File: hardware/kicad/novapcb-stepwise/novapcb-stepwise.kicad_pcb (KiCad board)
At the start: 6 copper layers, 105 x 85 mm, 129 parts, among them J1 USB-C_2.0, J10 CRSF_solder_pad, J11 ESC_solder_pad, J12 ESC_solder_pad, J13 ESC_solder_pad, J14 ESC_solder_pad, J15 ESC_solder_pad, J16 ESC_solder_pad, J17 ESC_solder_pad, J18 ESC_solder_pad, J19 MAUCH2_6P, J2 microSD_DM3AT, J20 CAN_4P, J3 TELEM_6P, J4 MAUCH_6P, J5 GPS_MAG_10P, J9 SWD_10P, Q2 AO3401A, Q3 AO4262E, Q4 AO4262E, Q5 AO3400A, U1 STM32H743VITx, U11 LM74700-Q1, U12 LM74700-Q1, U13 LP5907MFX-3.3, U14 TJA1051TK/3, U15 PESD2CAN, U2 AP2112K-3.3, U3 ICM-42688-P_LGA-14_2.5x3mm_P0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, U4 DPS310, U5 USBLC6-2P6, U6 TPS25940A, U7 LPS22HB, U8 BMI088, U9 LSM6DSV16X, Y1 8MHz

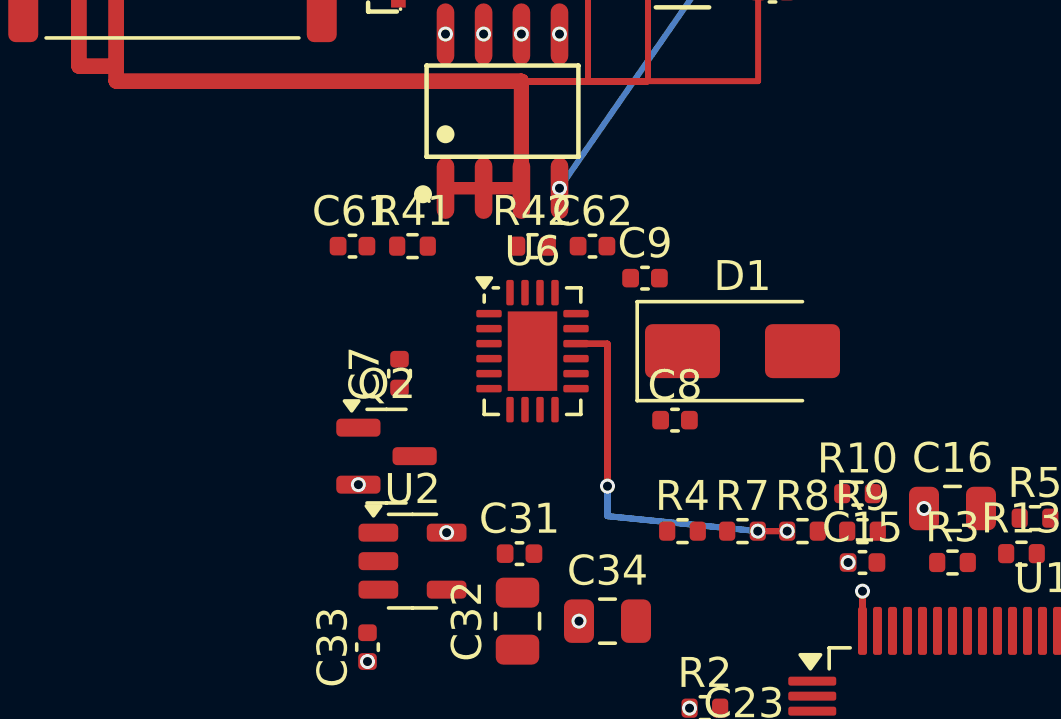
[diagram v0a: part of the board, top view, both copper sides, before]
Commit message: hw: R42/C62 west-relocate per master Option (selective B re-place)
Per master 2026-05-23 selective relocation approval after routing-
aware-density paper analysis.

## Move
  R42: (28.00, 14.50) → (20.00, 14.50) — 8mm west
  C62: (30.00, 14.50) → (18.00, 14.50) — 12mm west

Both moves CLEAR X=27..30 strip at Y=14.5 (U6's north-pin exit
column).

## Routing-aware-density verification (paper, executed pre-move)
All 4 EFUSE routes verified geometrically possible with new positions
in the basic-clearance sense. R42 no longer blocks DVDT/ILIM/FLT exits.

## Post-execute DRC: 11 violations (down from blocked)

Sense-row blockers RESOLVED. But other geometric conflicts surfaced
that the basic-clearance verification missed:
  - OVP F.Cu trace at X=31.5 too close to D1 pad west edge 31.75
    (gap 0.15mm vs 0.20mm rule). Needs via X<31.45.
  - ILIM B.Cu diagonal (28.75, 14.5)→(32.49, 24) passes within
    0.37mm of OVP via center at (31.5, 22.5) — 0.02mm edge-to-edge
    fail.
  - DVDT via at (28.25, 13) too close to Q3.3 pad (27.63, 12.57)
    — 0.75mm vs 1.05mm clearance need (via 0.25 + pad 0.6 + clr 0.2).
  - ILIM via at (28.75, 14.5) too close to DVDT F.Cu at X=28.25
    Y=14.5 (gap 0.15mm via-to-track edge).
  - EN B.Cu vs ILIM B.Cu cross in R-corridor.

These are SECOND-ORDER conflicts (placement of R42/C62 was the
first-order; now the routing-routing collisions and Q3/D1 adjacency
need addressing).

ESCALATING — multiple targeted routing iterations needed OR more
placement nudges (R4 east, OVP via re-position, etc).

## Sequence ask
Master direction needed on iteration approach: keep iterating routing
under no-new-fab-exceptions rule, or pause and assess whether one
more bounded placement change resolves all 4 cleanly.

Co-Authored-By: Claude Opus 4.7 <noreply@anthropic.com>
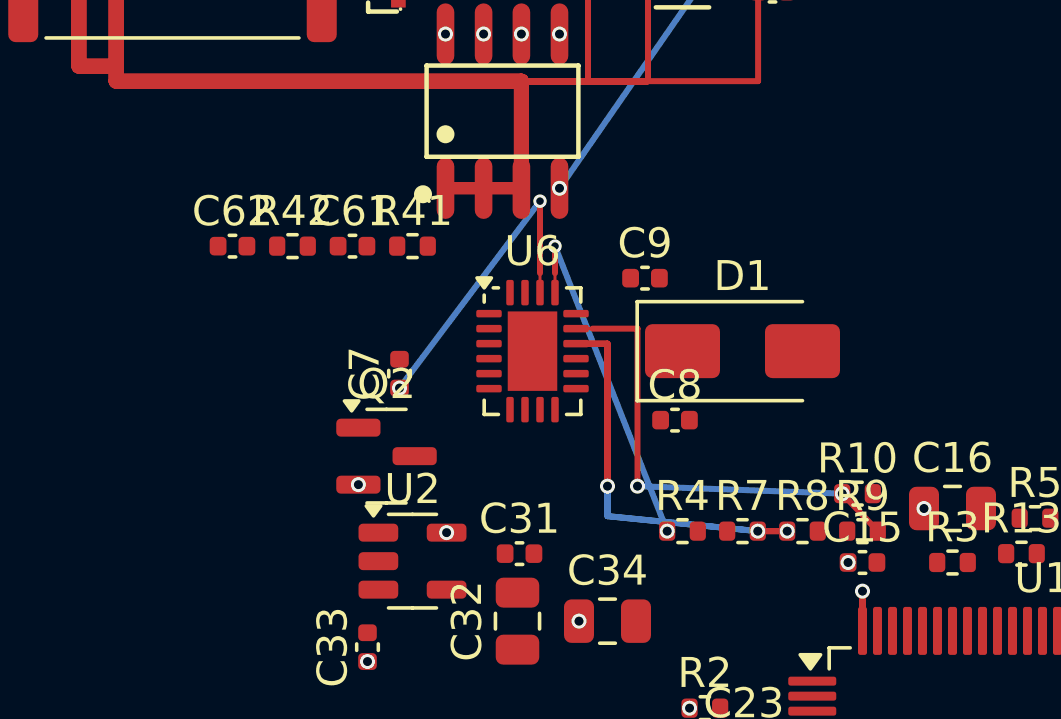
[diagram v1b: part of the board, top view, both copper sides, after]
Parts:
- moved C62 12.0 mm to (18.0, 14.5)
- moved R42 8.00 mm to (20.0, 14.5)
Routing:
- net EFUSE_OVP: track 0.00 -> 15.9 mm, vias 0 -> 2
- net EFUSE_ILIM: track 0.00 -> 11.8 mm, vias 0 -> 2
- net EFUSE_DVDT: track 0.00 -> 10.8 mm, vias 0 -> 2
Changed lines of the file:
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@@
 	(footprint "Capacitor_SMD:C_0402_1005Metric"
 		(layer "F.Cu")
-		(at 30 14.5)
+		(at 18 14.5)
 		(descr "Capacitor SMD 0402 (1005 Metric), square (rectangular) end terminal, IPC-7351 nominal, (Body size source: IPC-SM-782 page 76, https://www.pcb-3d.com/wordpress/wp-content/uploads/ipc-sm-782a_amendment_1_and_2.pdf), generated with kicad-footprint-generator")
 		(tags "capacitor")
@@
 	(footprint "Resistor_SMD:R_0402_1005Metric"
 		(layer "F.Cu")
-		(at 28 14.5)
+		(at 20 14.5)
 		(descr "Resistor SMD 0402 (1005 Metric), square (rectangular) end terminal, IPC-7351 nominal, (Body size source: IPC-SM-782 page 72, https://www.pcb-3d.com/wordpress/wp-content/uploads/ipc-sm-782a_amendment_1_and_2.pdf), generated with kicad-footprint-generator")
 		(tags "resistor")
@@
 	)
 	(segment
+		(start 28.25 16.05)
+		(end 28.25 15.4)
+		(width 0.1)
+		(layer "F.Cu")
+		(net 23)
+	)
+	(segment
+		(start 28.25 15.4)
+		(end 28.25 13)
+		(width 0.2)
+		(layer "F.Cu")
+		(net 23)
+	)
+	(via
+		(at 23.566987 19.23)
+		(size 0.5)
+		(drill 0.3)
+		(layers "F.Cu" "B.Cu")
+		(net 23)
+	)
+	(via
+		(at 28.25 13)
+		(size 0.45)
+		(drill 0.25)
+		(layers "F.Cu" "B.Cu")
+		(net 23)
+	)
+	(segment
+		(start 28.25 13)
+		(end 23.566987 19.23)
+		(width 0.2)
+		(layer "B.Cu")
+		(net 23)
+	)
+	(segment
 		(start 29.45 17.75)
 		(end 30.5 17.75)
@@
 	)
 	(segment
+		(start 28.75 16.05)
+		(end 28.75 15.4)
+		(width 0.1)
+		(layer "F.Cu")
+		(net 26)
+	)
+	(segment
+		(start 28.75 15.4)
+		(end 28.75 14.5)
+		(width 0.2)
+		(layer "F.Cu")
+		(net 26)
+	)
+	(via
+		(at 28.75 14.5)
+		(size 0.45)
+		(drill 0.25)
+		(layers "F.Cu" "B.Cu")
+		(net 26)
+	)
+	(via
+		(at 32.49 24)
+		(size 0.5)
+		(drill 0.3)
+		(layers "F.Cu" "B.Cu")
+		(net 26)
+	)
+	(segment
+		(start 28.75 14.5)
+		(end 32.49 24)
+		(width 0.2)
+		(layer "B.Cu")
+		(net 26)
+	)
+	(segment
+		(start 30 17.25)
+		(end 31.5 17.25)
+		(width 0.2)
+		(layer "F.Cu")
+		(net 27)
+	)
+	(segment
+		(start 31.5 17.25)
+		(end 31.5 22.5)
+		(width 0.2)
+		(layer "F.Cu")
+		(net 27)
+	)
+	(segment
+		(start 38.324936 22.75)
+		(end 39.51 24)
+		(width 0.2)
+		(layer "F.Cu")
+		(net 27)
+	)
+	(segment
+		(start 29.45 17.25)
+		(end 30 17.25)
+		(width 0.1)
+		(layer "F.Cu")
+		(net 27)
+	)
+	(via
+		(at 31.5 22.5)
+		(size 0.5)
+		(drill 0.3)
+		(layers "F.Cu" "B.Cu")
+		(net 27)
+	)
+	(via
+		(at 38.324936 22.75)
+		(size 0.5)
+		(drill 0.3)
+		(layers "F.Cu" "B.Cu")
+		(net 27)
+	)
+	(segment
+		(start 31.5 22.5)
+		(end 38.324936 22.75)
+		(width 0.2)
+		(layer "B.Cu")
+		(net 27)
+	)
+	(segment

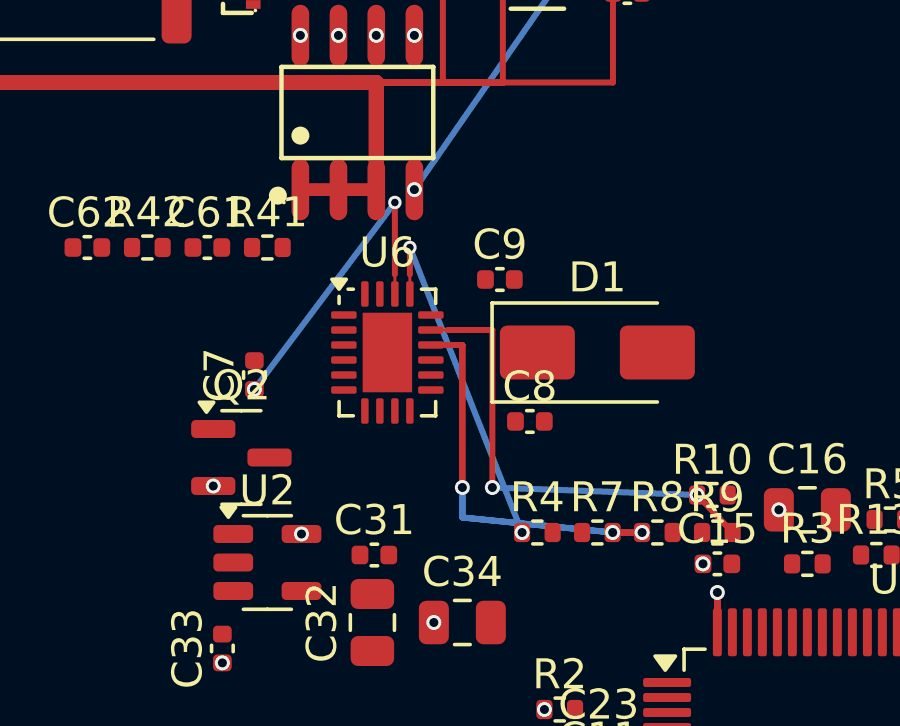
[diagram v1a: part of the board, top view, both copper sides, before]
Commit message: hw: U6 protection-config iter — converging, 3 borderline fails left
Per master 2026-05-23 Option (c) execution.

## Iteration sequence
  R4 placement: (33, 24) → (32, 22) → (31, 22) → (32.5, 22) → (34, 22)
  OVP via: (32, 22.5) → (31.5, 22.5) → (31.30, 22.5)
  DVDT via: (28.25, 13) → (24, 13) → (24, 13.10) → (22, 12.5)

## Current state — 3 borderline DRC fails

1. (22, 12.5) DVDT B.Cu dangling — endpoint at via, electrical via
   pad overlap valid (KiCad pedantic).
2. (31.30, 22.50) OVP B.Cu vs ILIM via clearance 0.174mm (need 0.20)
   — 0.026mm short. ILIM via from R4.1 still at OLD location
   (31.99, 22 = from R4 at 32.5 prior iteration). Strip didn't
   catch it; needs idempotent strip extension.
3. (25.10, 12.57) Q3.1 +5V_BEC_A vs DVDT F.Cu clearance 0.187mm
   — 0.013mm short. Track passes 0.21mm geometric distance from
   pad corner but KiCad reports 0.19mm (different metric perhaps
   includes pad expansion).

## Decision needed

Final 3 issues need:
  i. Extend strip to remove OLD ILIM via at (31.99, 22).
  ii. DVDT via further west OR finer Y adjustment to clear Q3.1
      0.013mm shortfall.
  iii. DVDT B.Cu dangling — investigate via connectivity.

Going to extend idempotent strip + final DVDT nudge next iteration.

Co-Authored-By: Claude Opus 4.7 <noreply@anthropic.com>
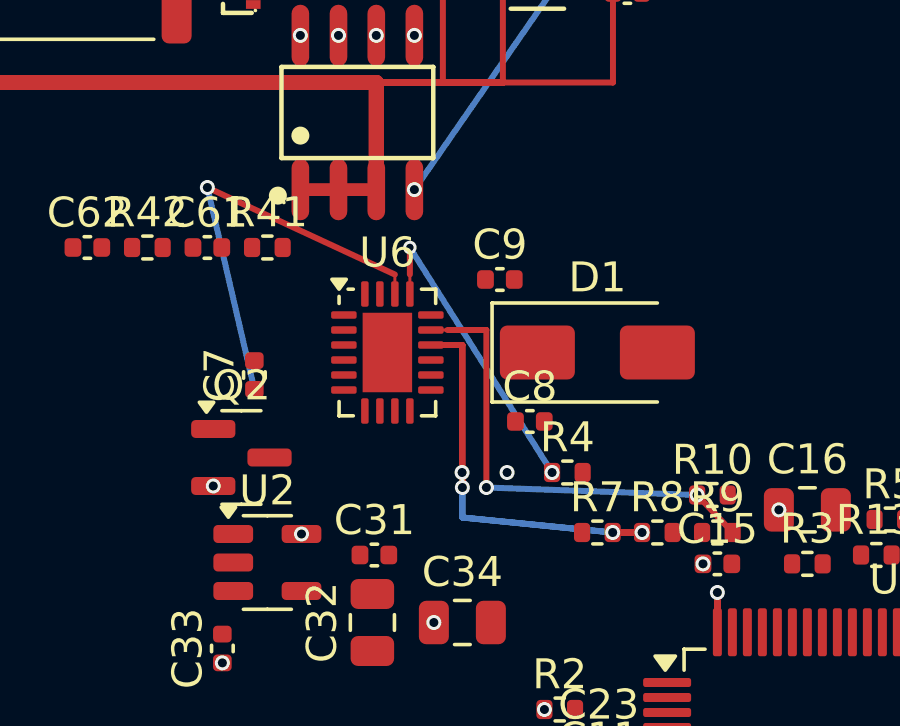
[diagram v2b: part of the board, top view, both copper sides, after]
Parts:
- moved R4 2.24 mm to (34.0, 22.0)
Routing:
- net EFUSE_DVDT: track 10.8 -> 14.5 mm, vias 2 -> 1
- net EFUSE_ILIM: track 11.8 -> 10.4 mm, vias 2 -> 3
- net EFUSE_EN: vias 3 -> 4
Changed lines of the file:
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@@
 	(footprint "Resistor_SMD:R_0402_1005Metric"
 		(layer "F.Cu")
-		(at 33 24)
+		(at 34 22)
 		(descr "Resistor SMD 0402 (1005 Metric), square (rectangular) end terminal, IPC-7351 nominal, (Body size source: IPC-SM-782 page 72, https://www.pcb-3d.com/wordpress/wp-content/uploads/ipc-sm-782a_amendment_1_and_2.pdf), generated with kicad-footprint-generator")
 		(tags "resistor")
@@
 	)
 	(segment
-		(start 28.25 16.05)
-		(end 28.25 15.4)
-		(width 0.1)
+		(start 28.25 15.4)
+		(end 22 12.5)
+		(width 0.2)
 		(layer "F.Cu")
 		(net 23)
 	)
 	(segment
-		(start 28.25 15.4)
-		(end 28.25 13)
-		(width 0.2)
+		(start 28.25 16.05)
+		(end 28.25 15.4)
+		(width 0.1)
 		(layer "F.Cu")
 		(net 23)
 	)
 	(via
-		(at 23.566987 19.23)
+		(at 22 12.5)
 		(size 0.5)
 		(drill 0.3)
@@
 		(net 23)
 	)
-	(via
-		(at 28.25 13)
-		(size 0.45)
-		(drill 0.25)
-		(layers "F.Cu" "B.Cu")
-		(net 23)
-	)
 	(segment
-		(start 28.25 13)
+		(start 22 12.5)
 		(end 23.566987 19.23)
 		(width 0.2)
@@
 	)
 	(via
+		(at 30.49 22)
+		(size 0.5)
+		(drill 0.3)
+		(layers "F.Cu" "B.Cu")
+		(net 24)
+	)
+	(via
 		(at 30.5 22.5)
 		(size 0.5)
@@
 	)
 	(segment
-		(start 28.75 16.05)
-		(end 28.75 15.4)
-		(width 0.1)
+		(start 28.75 15.4)
+		(end 28.75 14.5)
+		(width 0.2)
 		(layer "F.Cu")
 		(net 26)
 	)
 	(segment
-		(start 28.75 15.4)
-		(end 28.75 14.5)
-		(width 0.2)
+		(start 28.75 16.05)
+		(end 28.75 15.4)
+		(width 0.1)
 		(layer "F.Cu")
 		(net 26)
@@
 	)
 	(via
-		(at 32.49 24)
+		(at 31.99 22)
+		(size 0.5)
+		(drill 0.3)
+		(layers "F.Cu" "B.Cu")
+		(net 26)
+	)
+	(via
+		(at 33.49 22)
 		(size 0.5)
 		(drill 0.3)
@@
 	(segment
 		(start 28.75 14.5)
-		(end 32.49 24)
+		(end 33.49 22)
 		(width 0.2)
 		(layer "B.Cu")
@@
 	)
 	(segment
-		(start 30 17.25)
-		(end 31.5 17.25)
+		(start 38.324936 22.75)
+		(end 39.51 24)
 		(width 0.2)
 		(layer "F.Cu")
@@
 	)
 	(segment
-		(start 31.5 17.25)
-		(end 31.5 22.5)
-		(width 0.2)
+		(start 29.45 17.25)
+		(end 30 17.25)
+		(width 0.1)
 		(layer "F.Cu")
 		(net 27)
 	)
 	(segment
-		(start 38.324936 22.75)
-		(end 39.51 24)
+		(start 31.3 17.25)
+		(end 31.3 22.5)
 		(width 0.2)
 		(layer "F.Cu")
@@
 	)
 	(segment
-		(start 29.45 17.25)
-		(end 30 17.25)
-		(width 0.1)
+		(start 30 17.25)
+		(end 31.3 17.25)
+		(width 0.2)
 		(layer "F.Cu")
 		(net 27)
 	)
 	(via
-		(at 31.5 22.5)
+		(at 38.324936 22.75)
 		(size 0.5)
 		(drill 0.3)
@@
 	)
 	(via
-		(at 38.324936 22.75)
+		(at 31.3 22.5)
 		(size 0.5)
 		(drill 0.3)
@@
 	)
 	(segment
-		(start 31.5 22.5)
+		(start 31.3 22.5)
 		(end 38.324936 22.75)
 		(width 0.2)

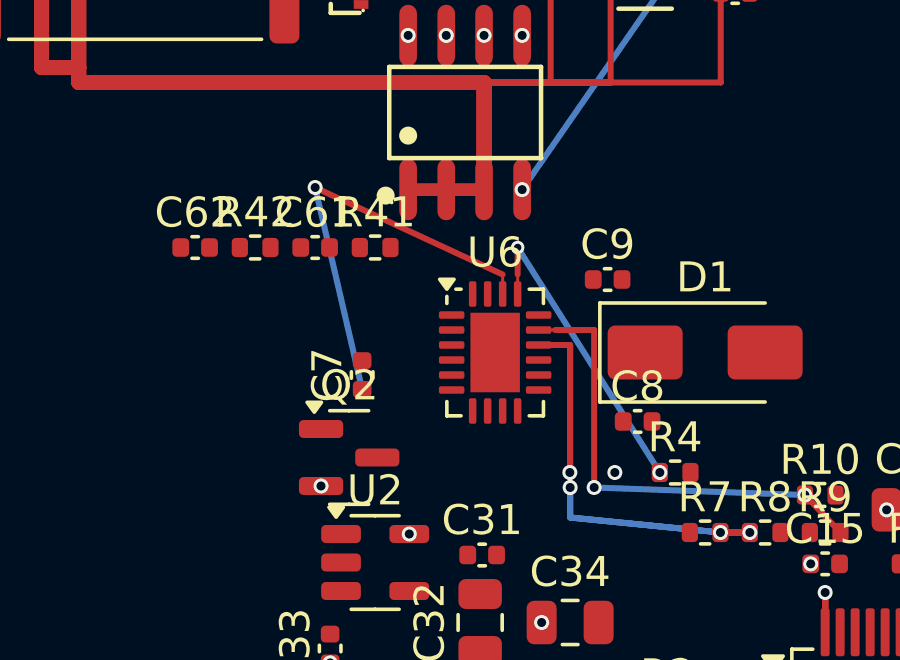
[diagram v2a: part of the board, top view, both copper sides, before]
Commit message: hw: U6 iter — DVDT via to (21, 12.5); 1 real issue left (R41.2 clearance 0.10)
Per master 2026-05-23 Option (c) continued iteration.

## DRC: 1 real issue + 2 KiCad-baseline + 1 KiCad-pedantic
  Real: DVDT F.Cu vs R41.2 pad clearance 0.0965mm (need 0.20mm).
  Baseline: I2C2 SCL/SDA dangling (master accepted KiCad-pedantic).
  Pedantic: DVDT B.Cu dangling at via (electrical OK).

## Geometric trap identified

DVDT F.Cu from U6.18 (28.25, 15.4) → via must pass between Q3.1 pad
(X=24.8..25.4 Y=11.5..13.6) and sense row R41/R42 pads (Y=13.98..15.02
at X=23.49..24.51 / 19.49..20.51).

The diagonal path has narrow safe corridor:
  - NORTH of Q3.1: Y < 11.5 — DVDT slope too shallow from (28.25, 15.4)
    to reach.
  - SOUTH of Q3.1 + NORTH of sense row: Y in 13.6..14.0 strip width
    0.4mm. Trace requires slope to land here at X=25..28.

Current path with via at (21, 12.5) → trace at X=24.51 Y=13.90 →
clips R41.2 pad north edge 13.98 by 0.02mm = effectively 0.0965mm
clearance fail.

## Solutions to consider (need master strategy)

  (1) Route DVDT SOUTH-around: via at (20, 16) — below sense row
      Y=15.0. Trace passes Y > 15.5 throughout. Clears Q3.1 + sense
      row entirely. Different B.Cu path from (20, 16) → C7.1 (23.57,
      19.23).
  (2) Route DVDT 4mil east-then-south: U6.18 east-exit through
      OVP/ILIM gap → south past C8 → west to C7.1. Many segments.
  (3) Move R41 east 1mm (R41 (24, 14.5) → (25, 14.5))? But then
      R41.1 collides with Q3.1 east edge X=25.4. No.
  (4) Move C7 — but C7 placement at (23.57, 19.23) is fixed by U6
      adjacency (DVDT pin needs short to C7).

Recommend (1) — route SOUTH-around. Cleanest geometric escape.

## Progress

From 11 DRC fails at iteration 0 → 1 real fail now.

Co-Authored-By: Claude Opus 4.7 <noreply@anthropic.com>
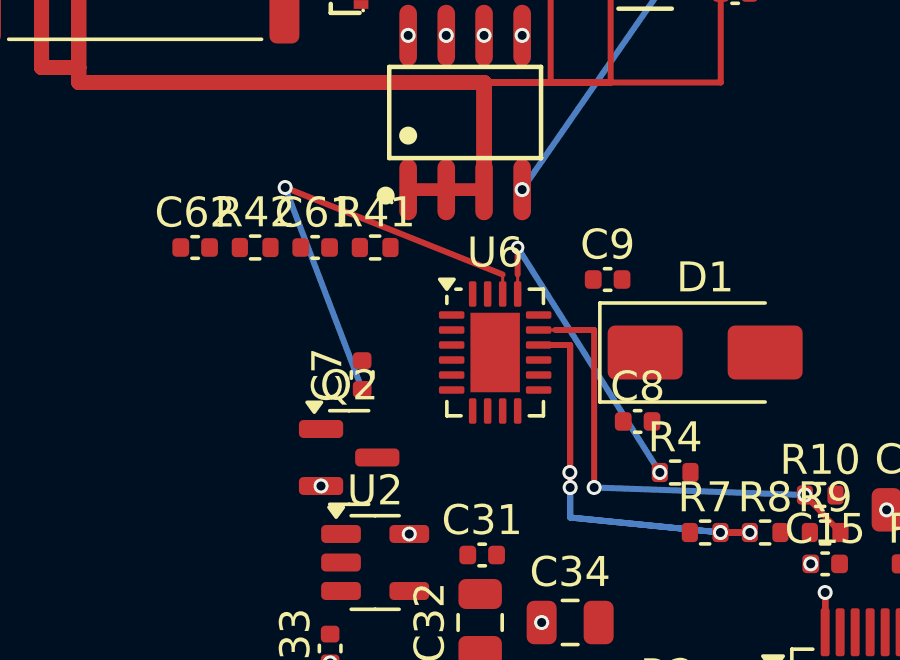
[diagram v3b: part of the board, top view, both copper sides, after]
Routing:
- net EFUSE_DVDT: track 14.5 -> 15.7 mm
- net EFUSE_ILIM: vias 3 -> 2
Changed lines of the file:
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@@
 	(segment
 		(start 28.25 15.4)
-		(end 22 12.5)
+		(end 21 12.5)
 		(width 0.2)
 		(layer "F.Cu")
@@
 	)
 	(via
-		(at 22 12.5)
-		(size 0.5)
-		(drill 0.3)
-		(layers "F.Cu" "B.Cu")
-		(net 23)
-	)
-	(segment
-		(start 22 12.5)
+		(at 21 12.5)
+		(size 0.5)
+		(drill 0.3)
+		(layers "F.Cu" "B.Cu")
+		(net 23)
+	)
+	(segment
+		(start 21 12.5)
 		(end 23.566987 19.23)
 		(width 0.2)
@@
 		(layer "B.Cu")
 		(net 24)
-	)
-	(segment
-		(start 28.75 15.4)
-		(end 28.75 14.5)
-		(width 0.2)
-		(layer "F.Cu")
-		(net 26)
 	)
 	(segment
@@
 		(net 26)
 	)
+	(segment
+		(start 28.75 15.4)
+		(end 28.75 14.5)
+		(width 0.2)
+		(layer "F.Cu")
+		(net 26)
+	)
 	(via
 		(at 28.75 14.5)
@@
 	)
 	(via
-		(at 31.99 22)
-		(size 0.5)
-		(drill 0.3)
-		(layers "F.Cu" "B.Cu")
-		(net 26)
-	)
-	(via
 		(at 33.49 22)
 		(size 0.5)
@@
 		(layer "B.Cu")
 		(net 26)
-	)
-	(segment
-		(start 38.324936 22.75)
-		(end 39.51 24)
-		(width 0.2)
-		(layer "F.Cu")
-		(net 27)
 	)
 	(segment
@@
 	)
 	(segment
+		(start 38.324936 22.75)
+		(end 39.51 24)
+		(width 0.2)
+		(layer "F.Cu")
+		(net 27)
+	)
+	(segment
 		(start 31.3 17.25)
 		(end 31.3 22.5)
@@
 	)
 	(via
+		(at 31.3 22.5)
+		(size 0.5)
+		(drill 0.3)
+		(layers "F.Cu" "B.Cu")
+		(net 27)
+	)
+	(via
 		(at 38.324936 22.75)
 		(size 0.5)
 		(drill 0.3)
-		(layers "F.Cu" "B.Cu")
-		(net 27)
-	)
-	(via
-		(at 31.3 22.5)
-		(size 0.5)
-		(drill 0.3)
